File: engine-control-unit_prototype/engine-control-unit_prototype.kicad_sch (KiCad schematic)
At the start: 167 parts, among them IC1 TPS259573DSGR, J1 JTAG, J10 PORT_B, J11 PORT_C, J12 PORT_D, J13 PORT_A, J14 PORT_G, J15 PORT_F, J16 PORT_E, J17 2S_18650, J2 USB_C_Receptacle_USB2.0_man, J3 Micro_SD_Card_Det1, J4 PT1, J5 VREF, J6 PT1, J7 VREF, J8 FDCAN, U1 USBLC6-2SC6, U13 INA219AxD, U14 LT3042xMSE, U3 INA826, U4 INA826, U5 TCAN337G, U6 INA219AxD, U7 STM32H747II, U8 INA219AxD, Y1 32.768KHz, Y2 25MHz

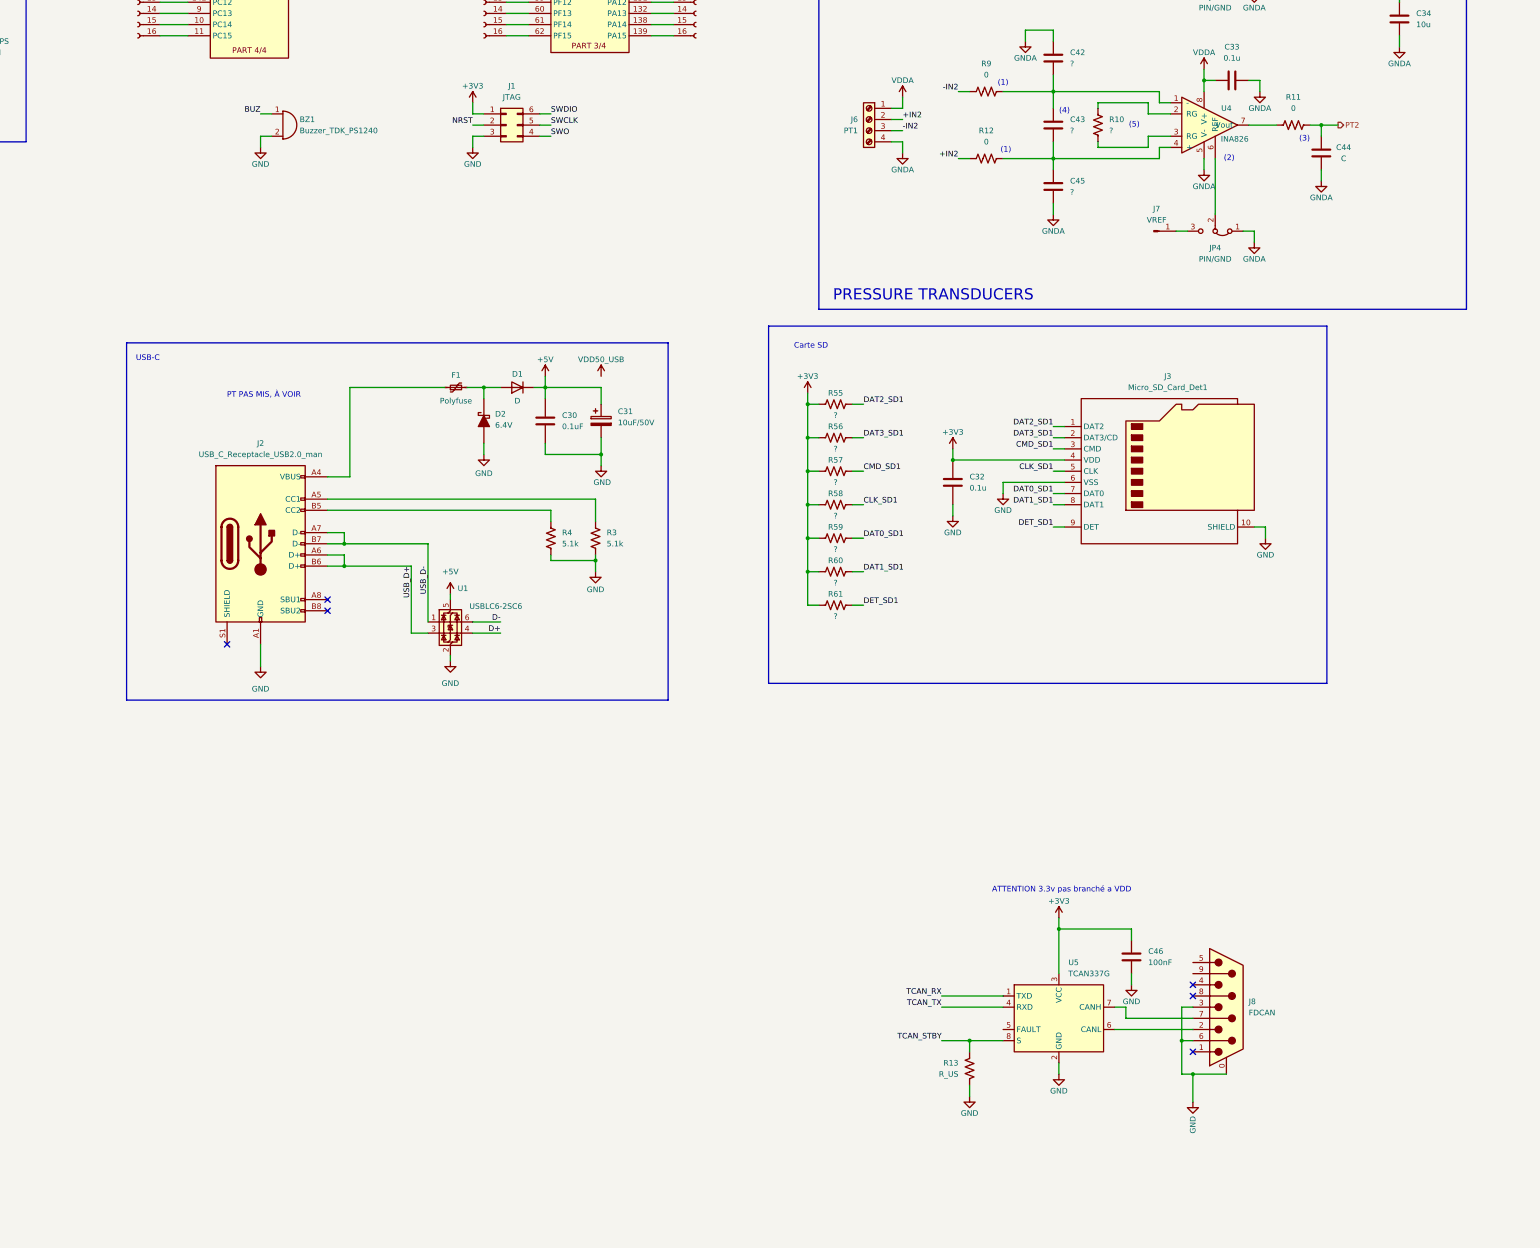
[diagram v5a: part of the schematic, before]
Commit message: Added ringing resistor for eMMC
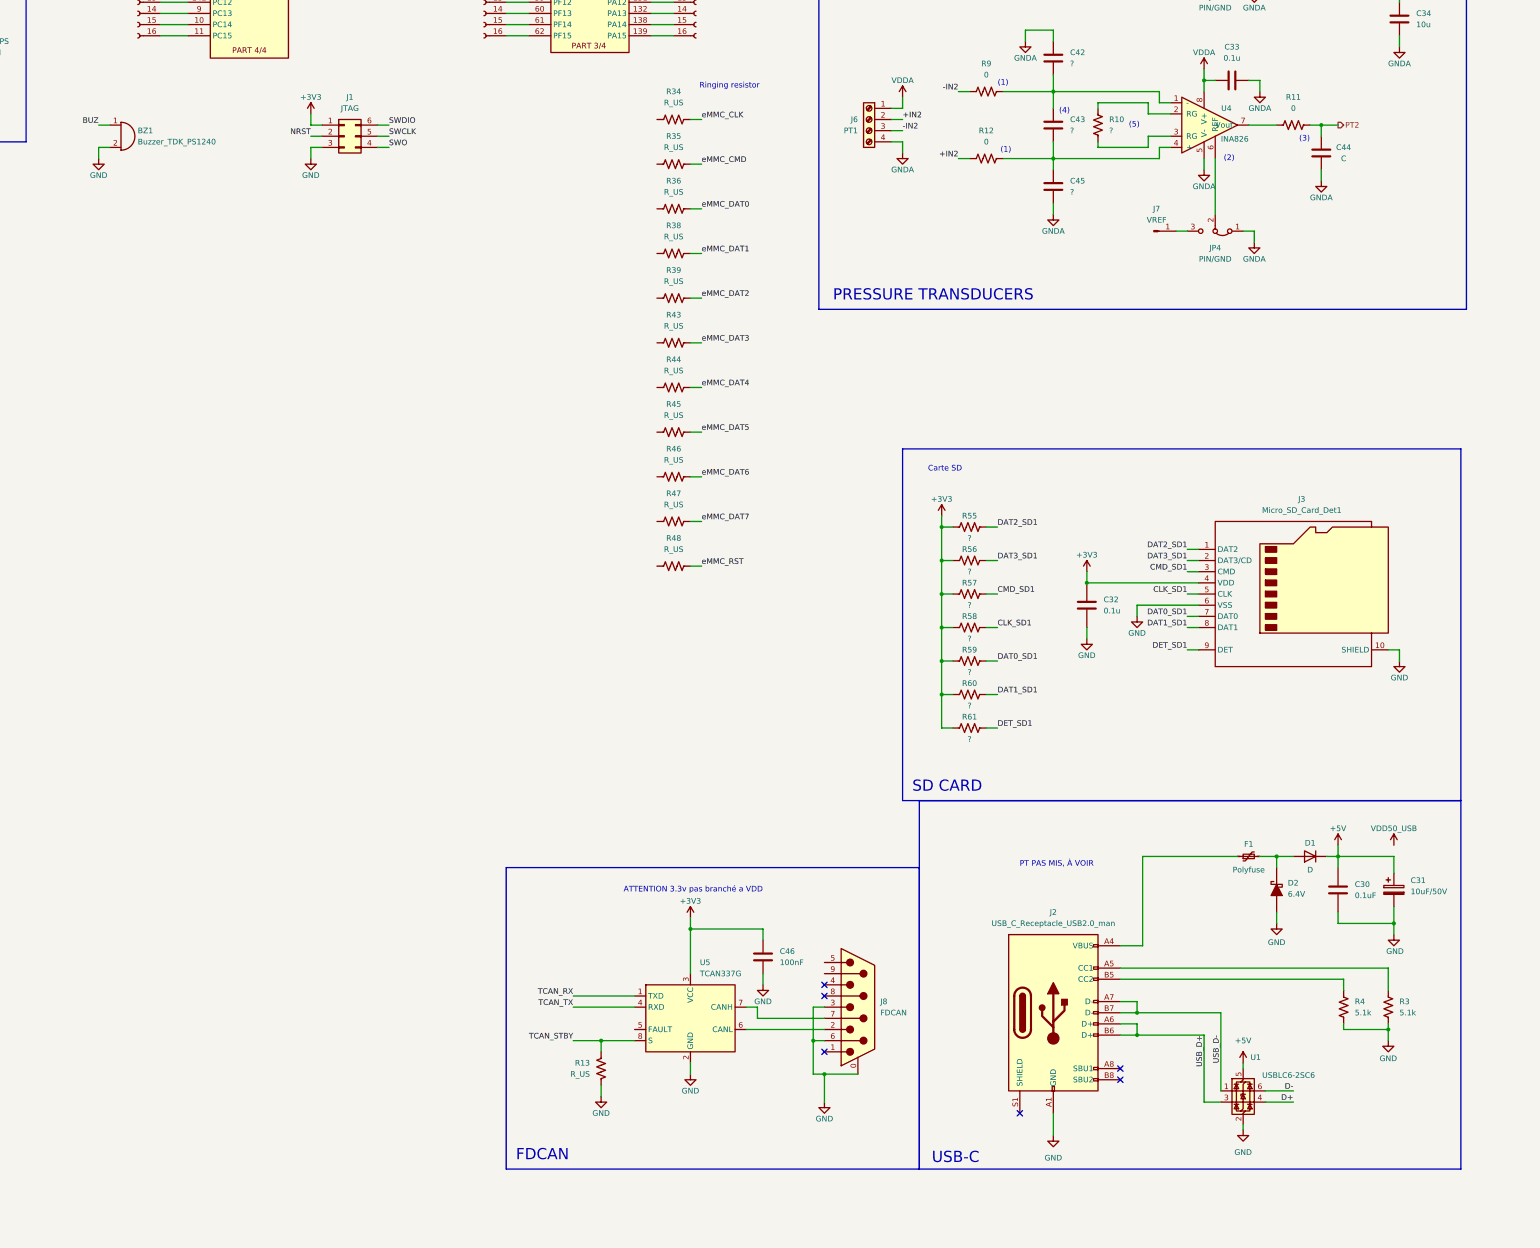
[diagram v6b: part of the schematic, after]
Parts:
- added R34, R35, R36, R38, R39, R43, R44, R45, R46, R47, R48: R_US, symbol Device:R_US
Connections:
- net eMMC_CLK: now also R34.2, R35.2
- net eMMC_DAT0: now also R36.2
- net eMMC_DAT1: now also R38.2
- net eMMC_DAT2: now also R39.2
- net eMMC_DAT3: now also R43.2
- net eMMC_DAT4: now also R44.2
- net eMMC_DAT5: now also R45.2
- net eMMC_DAT6: now also R46.2
- net eMMC_DAT7: now also R47.2
- net eMMC_RST: now also R48.2
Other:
- note added: "FDCAN"
- note added: "Ringing resistor"
- note added: "SD CARD"
- moved on the sheet: BZ1, C30, C31, C32, C46, D1, D2, F1, J1, J2, J3, J8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

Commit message: Fixed awkward sd card pull-up resistors placement
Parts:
- removed C32: 0.1u, Capacitor_SMD:C_0603_1608Metric_Pad1.08x0.95mm_HandSolder, symbol 0CSL_D1_V1:CAP_100nF_50V_0603
- removed R55, R56, R57, R58, R59, R60, R61: ?, symbol Device:R_US
- added C61: 0.1u, symbol Device:C
- added R49, R50, R51, R52, R53, R54, R62: 10k, symbol Device:R_US
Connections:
- net +3V3: now also C61.2, R49.1, R50.1, R51.1, R52.1, R53.1, R54.1, R62.1
- net CLK_SD1: now also R52.2
- net CMD_SD1: now also R53.2
- net DAT0_SD1: now also R51.2
- net DAT1_SD1: now also R50.2
- net DAT2_SD1: now also R62.2
- net DAT3_SD1: now also R54.2
- net DET_SD1: now also R49.2
- net GND: now also C61.1
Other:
- note removed: "Carte SD"
- moved on the sheet: J3

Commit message: Added TPS55285 circuits
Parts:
- added C32, C62, C63, C64, C65, C66, C75, C76, C77, C78, C79, C80, C81, C82, C83, C84, C85: C, symbol Device:C
- added L1, L2: L, symbol Device:L
- added R55, R56, R57, R58, R59, R60, R61, R63, R64: R_US, symbol Device:R_US
- added U10, U9: TPS55285, symbol SiriusLib:TPS55285
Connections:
- net GND: now also U14.11 (GND), U14.8 (GND), C32.2, C62.2, C65.2, C66.2, C75.2, C76.2, C77.2, C78.2, C81.2, C82.2, C83.2, C84.2, C85.2, R55.2, R57.2, R59.2, R61.2, R64.2, U10.12 (AGND), U10.7 (PGND), U9.12 (AGND), U9.7 (PGND)
- net Psense2_IN+: now also C81.1, U10.9 (VOUT)
- net Psense3_IN+: now also U14.10 (OUT), U14.9 (OUTS), C78.1, R58.1
- net VBAT_SAFE: now also C62.1, C82.1, U10.5 (VIN), U9.5 (VIN)
- net at U14.1 (IN), U14.2 (IN): now also U14.3 (EN/UV), C65.1, C76.1, R60.1, U9.9 (VOUT)
- net at U14.4 (PG): now also R60.2
- net at U14.5 (ILIM): now also R61.1
- net at U14.6 (PGFB): now also R58.2, R59.1
- net at U14.7 (SET): now also C77.1, R57.1
- new net: C85.1, R63.2
- new net: C63.1, L1.1, U9.6 (SW1)
- new net: C63.2, U9.15 (BOOT1)
- new net: C64.1, L1.2, U9.8 (SW2)
- new net: C64.2, U9.14 (BOOT2)
- new net: C79.1, L2.1, U10.6 (SW1)
- new net: C79.2, U10.15 (BOOT1)
- new net: R55.1, U9.1 (MODE)
- new net: C66.1, R56.1, U9.11 (COMP)
- new net: C32.1, U9.13 (VCC)
- new net: R64.1, U10.1 (MODE)
- new net: C84.1, R63.1, U10.11 (COMP)
- new net: C83.1, U10.13 (VCC)
- new net: C80.2, U10.14 (BOOT2)
- new net: C80.1, L2.2, U10.8 (SW2)
- new net: C75.1, R56.2
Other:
- note added: "TPS55285"
- moved on the sheet: R41, R42, U14
